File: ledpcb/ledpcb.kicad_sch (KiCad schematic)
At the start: 11 parts, among them J1 Conn_01x02_Female, J2 Conn_01x04_Female, J3 Barrel_Jack, J4 Conn_01x04_Male, Q1 ME2306A, Q2 ME2306A, Q3 ME2306A, SW1 SW_Push, U1 SPX3819M5-L-3-3_TR, U2 ESP32-WROOM-32

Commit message: version
Signed-off-by: 3nt3 <gott@3nt3.de>
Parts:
- added R2, R3: 5K1, symbol Device:R
- added U3: TMP100, Package_TO_SOT_SMD:SOT-23-6, symbol Sensor_Temperature:TMP100
- SW1: footprint Button_Switch_SMD:SW_Push_1P1T_NO_CK_KSC6xxJ -> easyeda2kicad:KEY-SMD_4P-L6.2-W6.5-P4.50-LS8.0_SKHMXX
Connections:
- net +3V3: now also R2.1, R3.1, U3.4 (V+)
- net GND: now also U3.2 (GND), U3.3 (ADD1), U3.5 (ADD0)
- net RED_CHANNEL: now also U2.29 (IO5); no longer U2.23 (IO15)
- net SDA: now reaches U2.33 (IO21)
- net SDA: now also R3.2, U3.6 (SDA)
- net SCL: now reaches U2.36 (IO22)
- net SCL: now also R2.2, U3.1 (SCL)
- no-connect marks 27 -> 25

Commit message: progress
Signed-off-by: 3nt3 <gott@3nt3.de>
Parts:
- J1: footprint (none) -> Connector_PinHeader_1.27mm:PinHeader_1x02_P1.27mm_Vertical
- J2: footprint (none) -> Connector_PinHeader_2.00mm:PinHeader_1x04_P2.00mm_Horizontal
- J3: footprint (none) -> Library:DEALON DC-S050-200
- R2, R3: footprint (none) -> Resistor_SMD:R_0603_1608Metric_Pad0.98x0.95mm_HandSolder
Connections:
- net +5V: now also J4.1 (Pin_1); no longer Q1.2 (S), Q2.2 (S), Q3.2 (S)
- net GND: now also Q1.2 (S), Q2.2 (S), Q3.2 (S); no longer J4.1 (Pin_1)
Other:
- moved on the sheet: J4, Q1, Q2, Q3

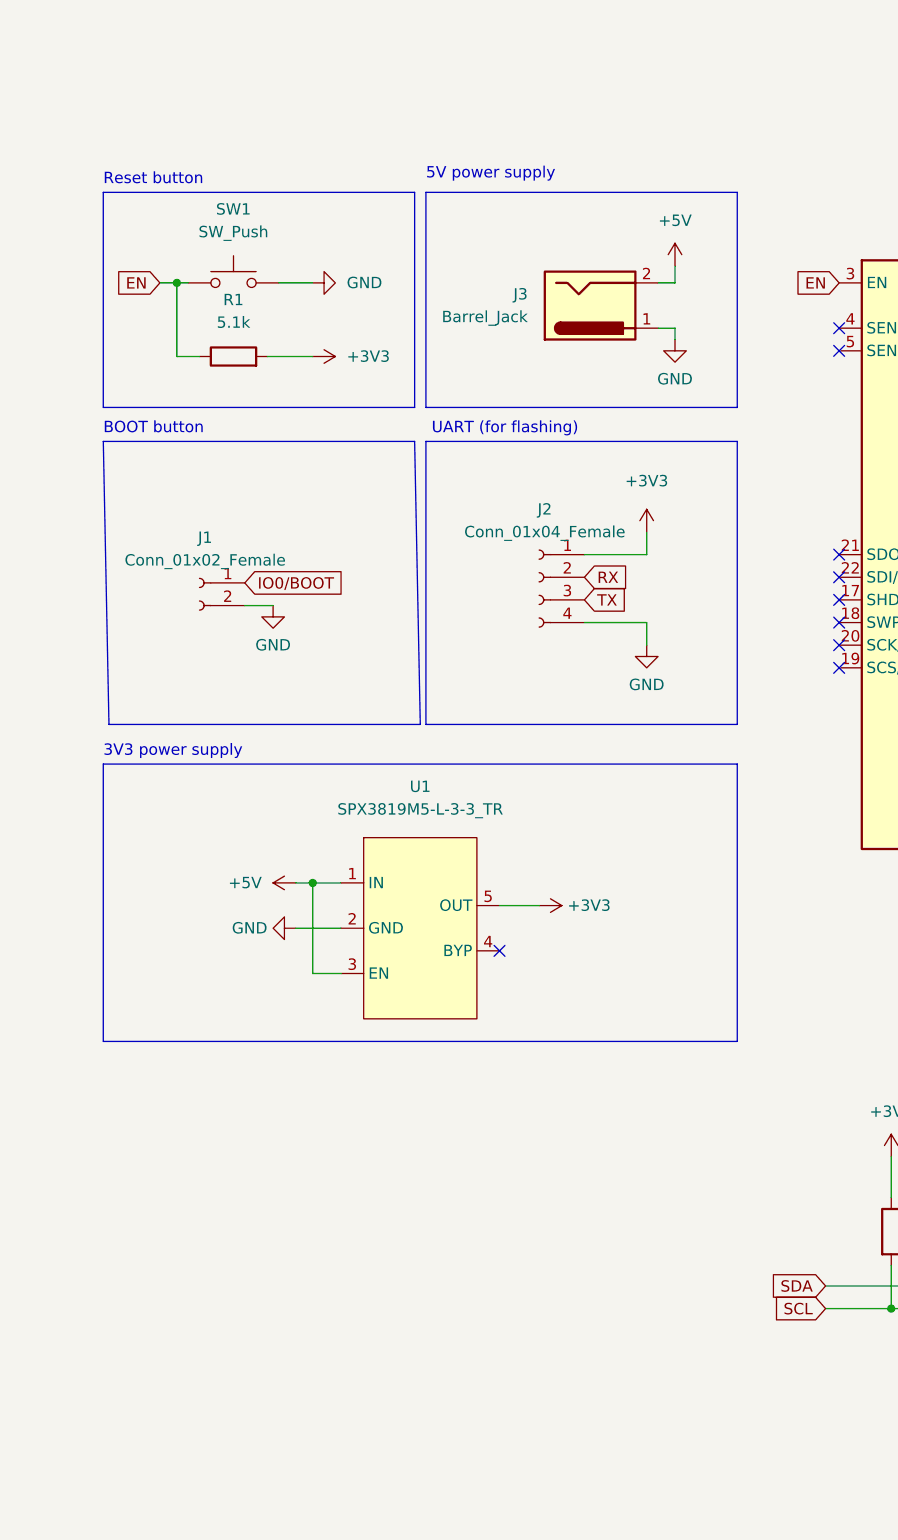
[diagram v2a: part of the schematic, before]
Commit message: add usb c receptable
Signed-off-by: 3nt3 <gott@3nt3.de>
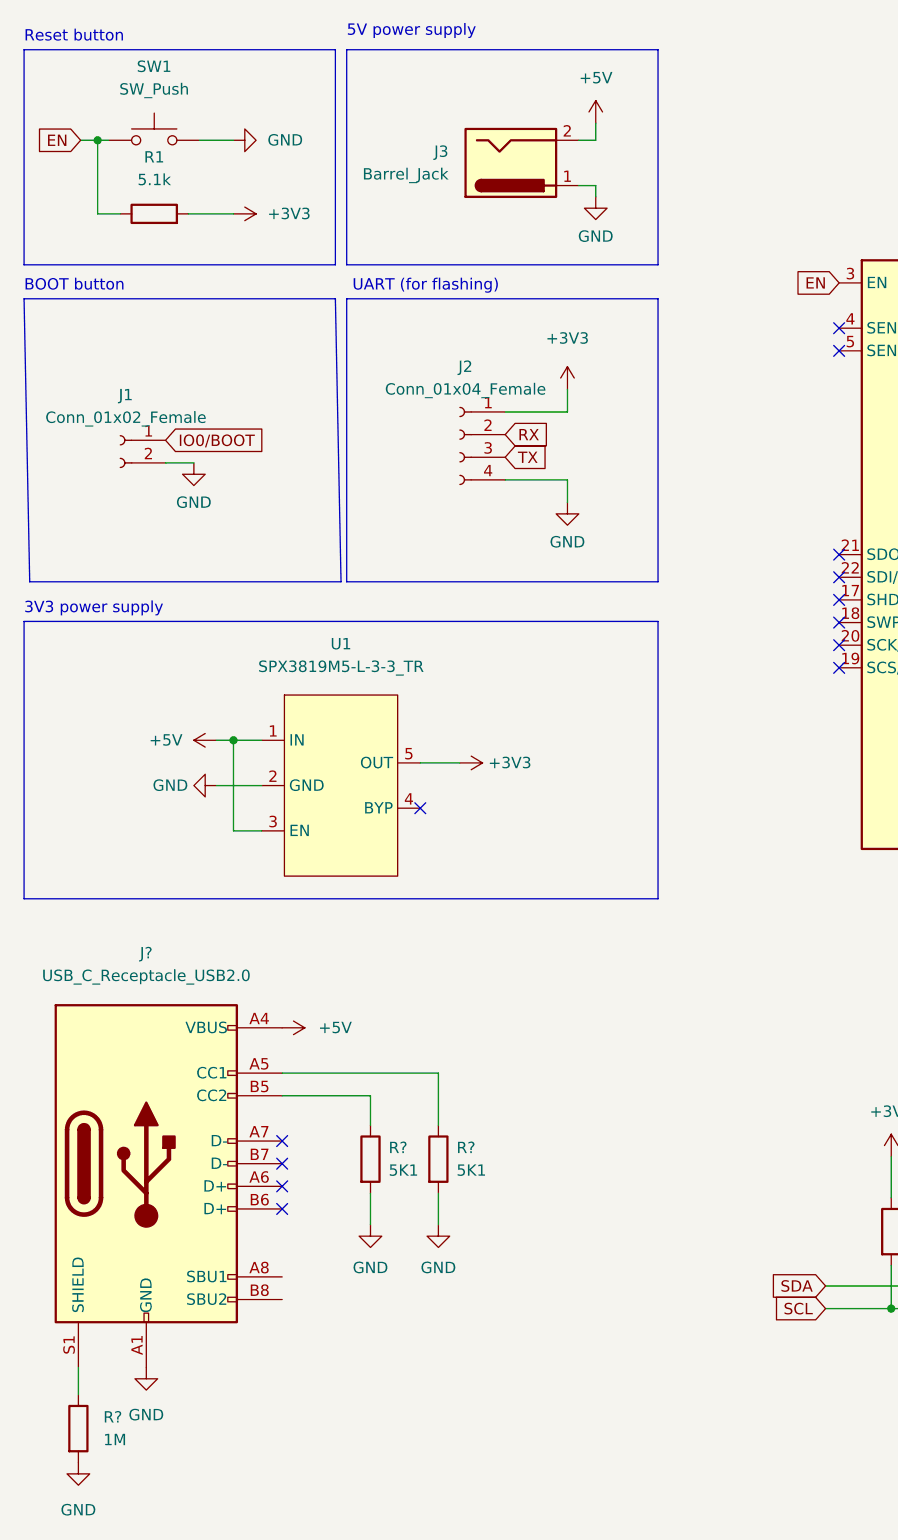
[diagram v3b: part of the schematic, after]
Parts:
- added J?: USB_C_Receptacle_USB2.0, symbol Connector:USB_C_Receptacle_USB2.0
- added R?: 1M, symbol Device:R
- added R? (x2): 5K1, symbol Device:R
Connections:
- net +5V: now also J?.A4 (VBUS), J?.A9 (VBUS), J?.B4 (VBUS), J?.B9 (VBUS)
- net GND: now also J?.A1 (GND), J?.A12 (GND), J?.B1 (GND), J?.B12 (GND), R?.2, R?.2, R?.2
- new net: J?.S1 (SHIELD), R?.1
- new net: J?.A5 (CC1), R?.1
- new net: J?.B5 (CC2), R?.1
- no-connect marks 25 -> 29
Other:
- moved on the sheet: J1, J2, J3, R1, SW1, U1

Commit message: fix traces or something
Signed-off-by: 3nt3 <gott@3nt3.de>
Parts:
- J2: renamed from J?; footprint (none) -> Connector_USB:USB_C_Receptacle_Palconn_UTC16-G
- R1: footprint Resistor_SMD:R_1206_3216Metric_Pad1.30x1.75mm_HandSolder -> Resistor_SMD:R_0603_1608Metric_Pad0.98x0.95mm_HandSolder
- R2, R3, R4: renamed from R?; footprint (none) -> Resistor_SMD:R_0603_1608Metric_Pad0.98x0.95mm_HandSolder
- renumbered J2 to J3, J3 to J4, J4 to J5, R2 to R5, R3 to R6
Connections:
- no-connect marks 29 -> 31
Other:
- moved on the sheet: J2, R2, R3, R4

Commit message: final?
Signed-off-by: 3nt3 <gott@3nt3.de>
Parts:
- R1: value 5.1k -> 5K1
- R2: footprint Resistor_SMD:R_0603_1608Metric_Pad0.98x0.95mm_HandSolder -> Resistor_SMD:R_2512_6332Metric_Pad1.40x3.35mm_HandSolder
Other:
- note added: "BOOT thingy"
- note removed: "BOOT button"
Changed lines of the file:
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@@
     (effects (font (size 1.27 1.27)) (justify left bottom))
   )
-  (text "BOOT button\n" (at 20.32 48.133 0)
+  (text "BOOT thingy\n" (at 20.32 48.133 0)
     (effects (font (size 1.27 1.27)) (justify left bottom))
   )
@@
       (effects (font (size 1.27 1.27)) (justify left))
     )
-    (property "Footprint" "Resistor_SMD:R_0603_1608Metric_Pad0.98x0.95mm_HandSolder" (id 2) (at 33.782 175.514 90)
+    (property "Footprint" "Resistor_SMD:R_2512_6332Metric_Pad1.40x3.35mm_HandSolder" (id 2) (at 33.782 175.514 90)
       (effects (font (size 1.27 1.27)) hide)
     )
@@
   (symbol (lib_id "Device:R") (at 34.925 39.243 90) (unit 1)
     (in_bom yes) (on_board yes) (fields_autoplaced)
-    (property "Reference" "R1" (id 0) (at 34.925 32.893 90))
-    (property "Value" "5.1k" (id 1) (at 34.925 35.433 90))
+    (property "Reference" "R1" (id 0) (at 34.925 33.02 90))
+    (property "Value" "5K1" (id 1) (at 34.925 35.56 90))
     (property "Footprint" "Resistor_SMD:R_0603_1608Metric_Pad0.98x0.95mm_HandSolder" (id 2) (at 34.925 41.021 90)
       (effects (font (size 1.27 1.27)) hide)
@@
     )
     (path "/e72c33c2-2b0d-4fd7-80a5-18c6fa851f43"
-      (reference "R1") (unit 1) (value "5.1k") (footprint "Resistor_SMD:R_0603_1608Metric_Pad0.98x0.95mm_HandSolder")
+      (reference "R1") (unit 1) (value "5K1") (footprint "Resistor_SMD:R_0603_1608Metric_Pad0.98x0.95mm_HandSolder")
     )
     (path "/016cea89-3d2b-4472-bb8e-5a77db197d0a"
-      (reference "R2") (unit 1) (value "1M") (footprint "Resistor_SMD:R_0603_1608Metric_Pad0.98x0.95mm_HandSolder")
+      (reference "R2") (unit 1) (value "1M") (footprint "Resistor_SMD:R_2512_6332Metric_Pad1.40x3.35mm_HandSolder")
     )
     (path "/ba36f504-e4c9-4f8f-9613-48b2947ecec8"

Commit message: whatever
Signed-off-by: 3nt3 <gott@3nt3.de>
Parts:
- J1: footprint Connector_PinHeader_1.27mm:PinHeader_1x02_P1.27mm_Vertical -> Connector_PinHeader_2.00mm:PinHeader_1x02_P2.00mm_Vertical
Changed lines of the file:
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@@
     (property "Reference" "J1" (id 0) (at 31.75 59.563 0))
     (property "Value" "Conn_01x02_Female" (id 1) (at 31.75 62.103 0))
-    (property "Footprint" "Connector_PinHeader_1.27mm:PinHeader_1x02_P1.27mm_Vertical" (id 2) (at 31.115 64.643 0)
+    (property "Footprint" "Connector_PinHeader_2.00mm:PinHeader_1x02_P2.00mm_Vertical" (id 2) (at 31.115 64.643 0)
       (effects (font (size 1.27 1.27)) hide)
     )
@@
     )
     (path "/89f7100f-f1cf-4330-8df9-8c60a680a26a"
-      (reference "J1") (unit 1) (value "Conn_01x02_Female") (footprint "Connector_PinHeader_1.27mm:PinHeader_1x02_P1.27mm_Vertical")
+      (reference "J1") (unit 1) (value "Conn_01x02_Female") (footprint "Connector_PinHeader_2.00mm:PinHeader_1x02_P2.00mm_Vertical")
     )
     (path "/bcaaa89d-39d9-4099-8fd8-7140c3fea82e"

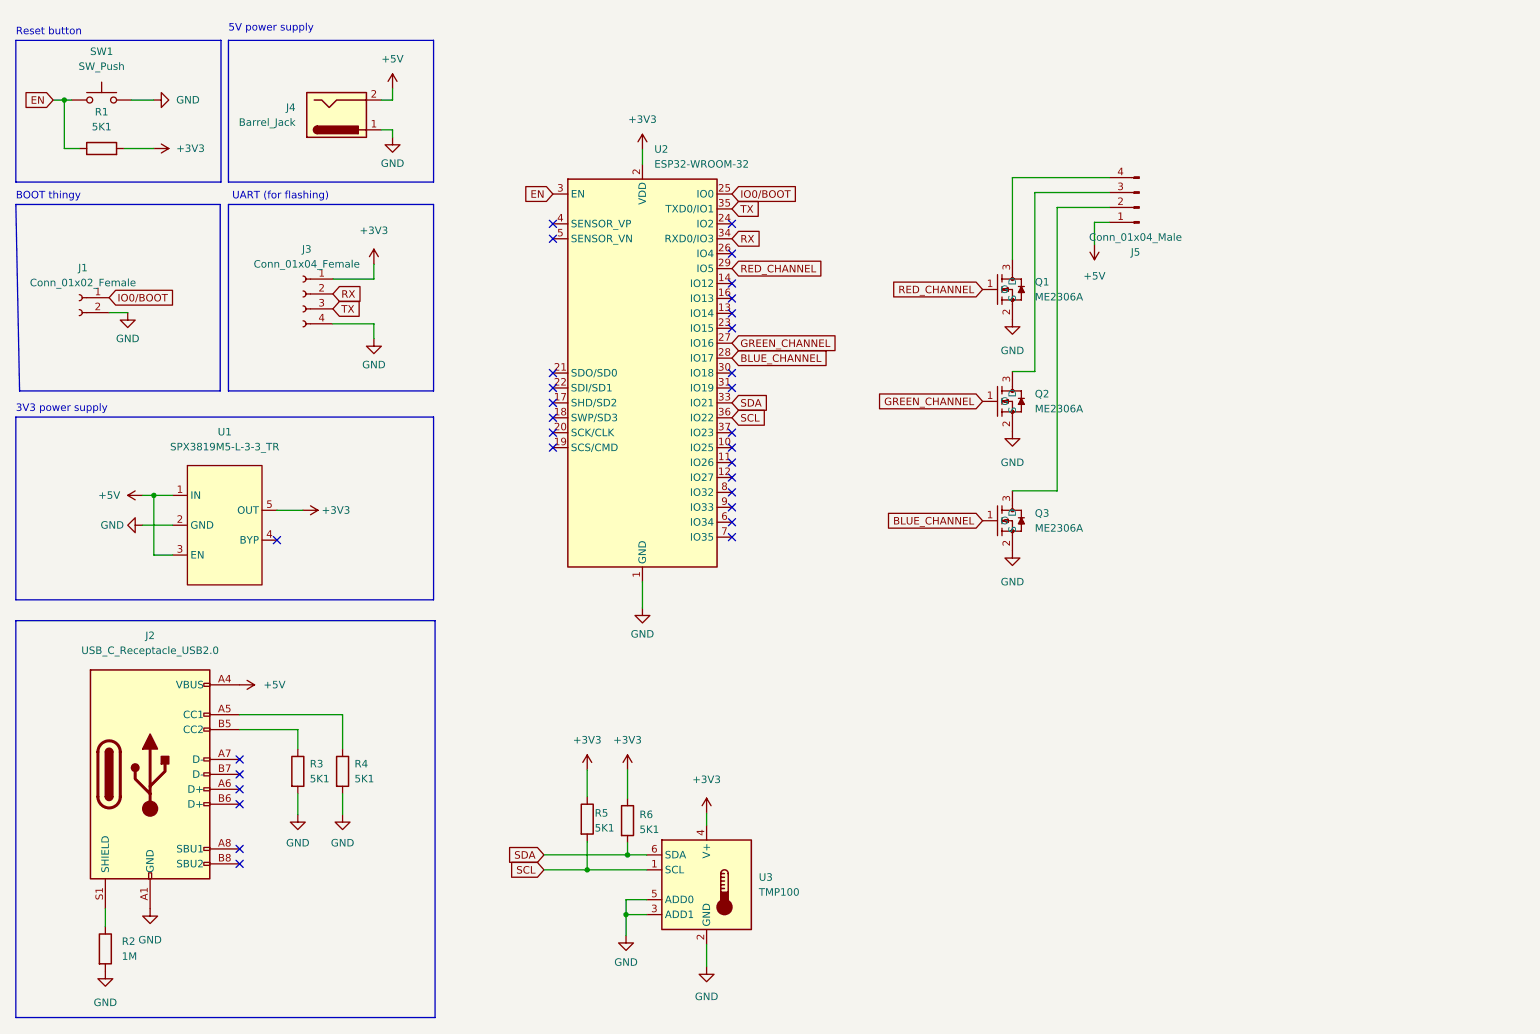
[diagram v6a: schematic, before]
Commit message: use esp32-s3
Signed-off-by: 3nt3 <gott@3nt3.de>
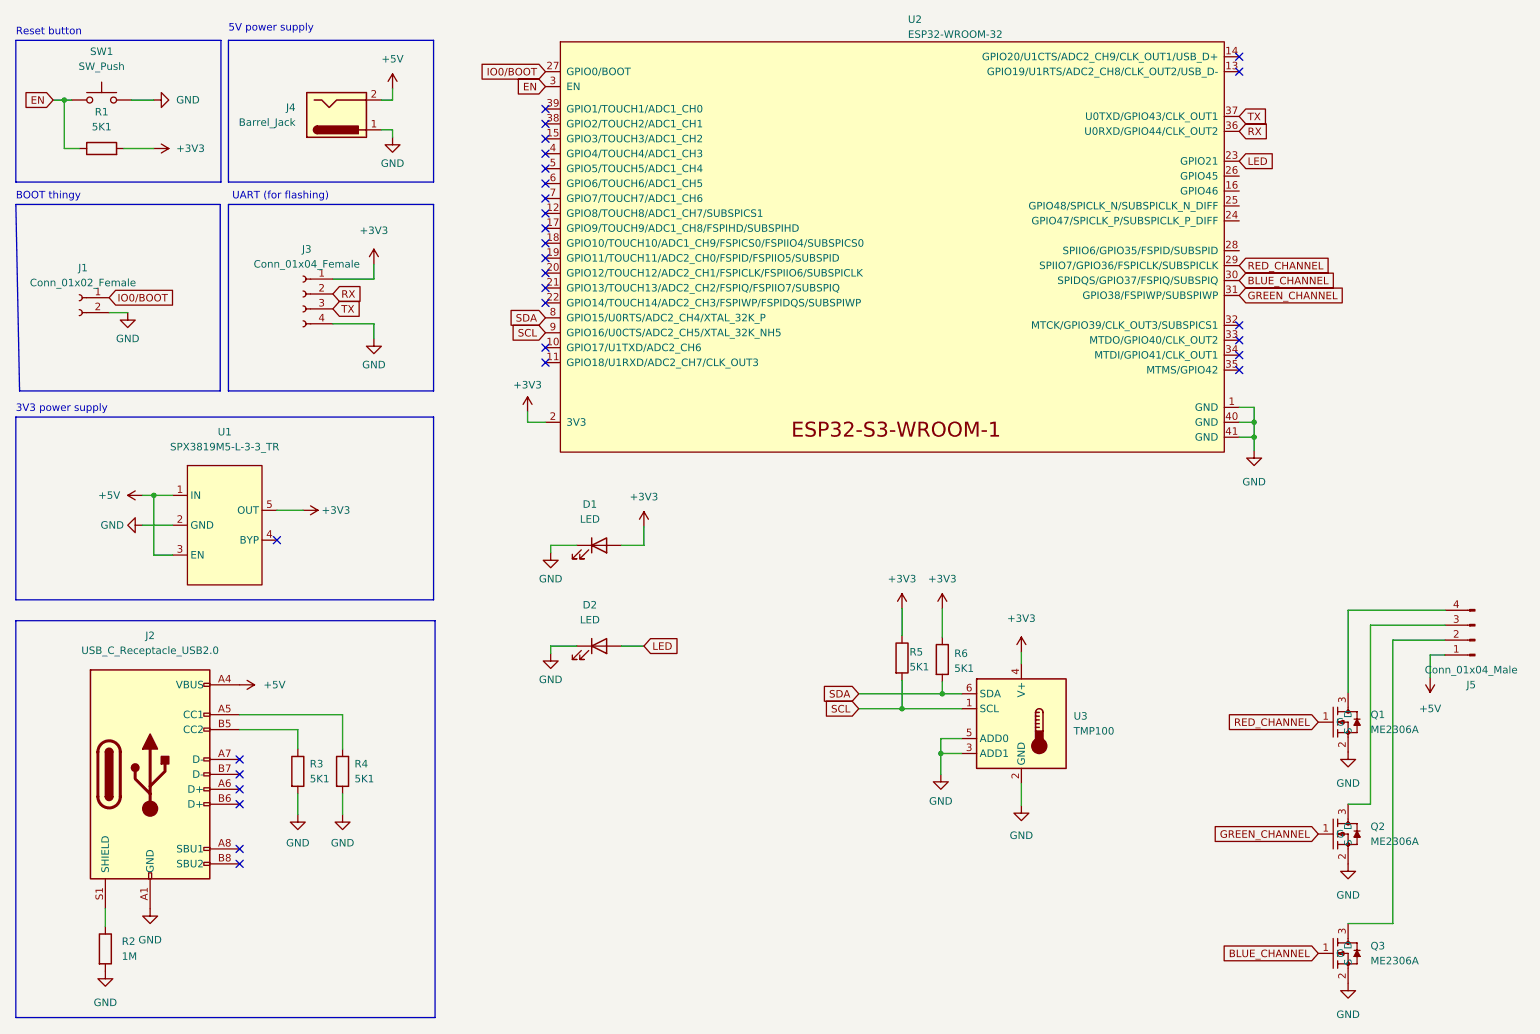
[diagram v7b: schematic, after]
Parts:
- added D1, D2: LED, symbol Device:LED
- U2: footprint RF_Module:ESP32-WROOM-32 -> Espressif:ESP32-S3-WROOM-1; symbol RF_Module:ESP32-WROOM-32 -> esp32:ESP32-S3-WROOM-1
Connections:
- net +3V3: now also D1.2 (A)
- net BLUE_CHANNEL: now also U2.30 (SPIDQS/GPIO37/FSPIQ/SUBSPIQ); no longer U2.28 (IO17)
- net GND: now also U2.40 (GND), U2.41 (GND), D1.1 (K), D2.1 (K); no longer U2.15 (GND), U2.38 (GND), U2.39 (GND)
- net GREEN_CHANNEL: now also U2.31 (GPIO38/FSPIWP/SUBSPIWP); no longer U2.27 (IO16)
- net IO0/BOOT: now also U2.27 (GPIO0/BOOT); no longer U2.25 (IO0)
- net RX: now also U2.36 (U0RXD/GPIO44/CLK_OUT2); no longer U2.34 (RXD0/IO3)
- net SCL: now also U2.9 (GPIO16/U0CTS/ADC2_CH5/XTAL_32K_NH5); no longer U2.36 (IO22)
- net SDA: now also U2.8 (GPIO15/U0RTS/ADC2_CH4/XTAL_32K_P); no longer U2.33 (IO21)
- net TX: now also U2.37 (U0TXD/GPIO43/CLK_OUT1); no longer U2.35 (TXD0/IO1)
- net LED: now reaches U2.23 (GPIO21)
- net LED: now also D2.2 (A)
- no-connect marks 31 -> 29
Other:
- moved on the sheet: J5, Q1, Q2, Q3, R5, R6, U3
